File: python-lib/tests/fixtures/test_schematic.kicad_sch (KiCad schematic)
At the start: 2 parts

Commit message: fix: complete phase 1 gaps - title_block, pin_uuids, wire topology nets, library & PCB tests
Agent-Logs-Url: https://github.com/mylonics/KiAssist/sessions/fecbef32-e4bb-4dd1-84e0-7b5318f435ac

Co-authored-by: rijesha <7819200+rijesha@users.noreply.github.com>
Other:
- company: (none) -> KiAssist
- title: (none) -> Test Schematic
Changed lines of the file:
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@@
 (kicad_sch (version 20231120) (generator "eeschema") (generator_version "8.0")
   (paper "A4")
+  (title_block
+    (title "Test Schematic")
+    (date "2026-04-03")
+    (rev "1.0")
+    (company "KiAssist")
+    (comment 1 "Top-level comment")
+    (comment 2 "")
+  )
   (wire (pts (xy 78.74 50.8) (xy 81.28 50.8))
     (stroke

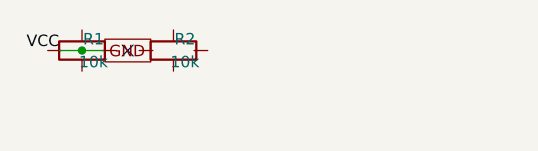
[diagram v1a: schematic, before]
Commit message: fix: KiCad 10 compatibility review — justify multi-word, effects hide, generator_version, sheet_pin, exclude_from_sim
Agent-Logs-Url: https://github.com/mylonics/KiAssist/sessions/d6c30cc2-8ed5-4125-80d6-521abce895de

Co-authored-by: rijesha <7819200+rijesha@users.noreply.github.com>
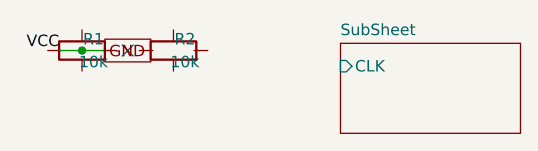
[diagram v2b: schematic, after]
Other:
- added sheet SubSheet (sub.kicad_sch)
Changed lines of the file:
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@@
     )
   )
-  (symbol (lib_id "Device:R") (at 81.28 50.8 90) (unit 1) (in_bom yes) (on_board yes)
+  (symbol (lib_id "Device:R") (at 81.28 50.8 90) (unit 1) (exclude_from_sim no) (in_bom yes) (on_board yes)
     (property "Reference" "R1" (at 82.5552 49.53 90)
       (effects
@@
     )
   )
-  (symbol (lib_id "Device:R") (at 91.44 50.8 90) (unit 1) (in_bom yes) (on_board yes)
+  (symbol (lib_id "Device:R") (at 91.44 50.8 90) (unit 1) (exclude_from_sim no) (in_bom yes) (on_board yes)
     (property "Reference" "R2" (at 92.7152 49.53 90)
       (effects
@@
     (pin "2")
   )
+  (sheet (at 110 50) (size 20 10)
+    (stroke (width 0) (type solid))
+    (fill (color 0 0 0 0.0000))
+    (property "Sheetname" "SubSheet" (at 110 48.5 0)
+      (effects
+        (font
+          (size 1.27 1.27)
+        )
+        (justify left)
+      )
+    )
+    (property "Sheetfile" "sub.kicad_sch" (at 110 61.0 0)
+      (effects
+        (font
+          (size 1.27 1.27)
+        )
+        (justify left)
+        (hide yes)
+      )
+    )
+    (pin "CLK" input (at 110 52.54 180)
+      (effects
+        (font
+          (size 1.27 1.27)
+        )
+      )
+    )
+  )
   (sheet_instances
